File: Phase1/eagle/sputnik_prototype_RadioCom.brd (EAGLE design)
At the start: 100 x 80 mm, 56 parts, among them Y1 32MHz

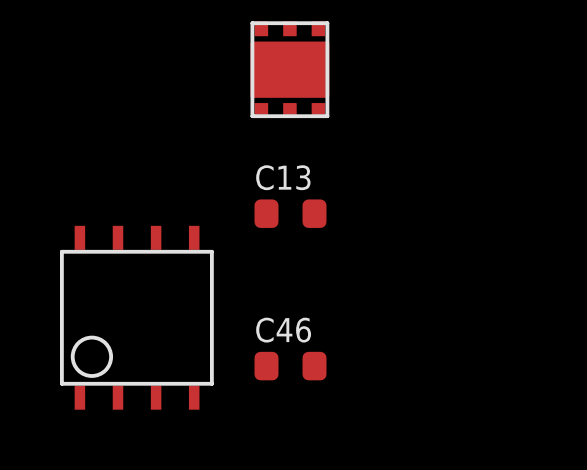
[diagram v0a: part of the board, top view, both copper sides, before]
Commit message: Added GPIOs and other updates on SysCon sch. Updated SPI cache footprint
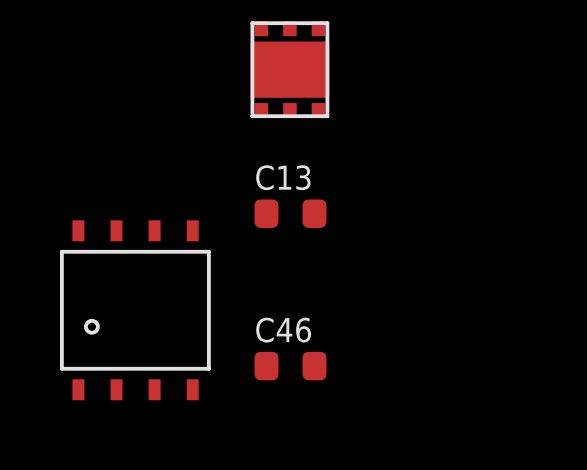
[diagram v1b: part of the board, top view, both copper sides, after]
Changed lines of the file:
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@@
 <?xml version="1.0" encoding="utf-8"?>
 <!DOCTYPE eagle SYSTEM "eagle.dtd">
-<eagle version="7.5.0">
+<eagle version="7.4.0">
 <drawing>
 <settings>
